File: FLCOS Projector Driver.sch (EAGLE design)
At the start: 64 parts, among them IC2 LM3414, IC3 MIC5219BM5, IC4 MIC5219BM5, IC5 LM3414, IC6 LM3414, Q1 14.31818MHz, Q3 12MHz, T2 S8050, T3 S8050, U1 TVP5150-NTSC_DECODER, U2 ESP32-WROOM-32U, U9 CH340G, X1 FH12-25S-0.5SH

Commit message: Started BOM. Changing parts to Mouser in-stock
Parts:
- removed Q1: 14.31818MHz, crystal:CRYSTALCTS406
- removed T3: S8050, transistor:BC846
- removed U$10: MICROSD, micro-sd:MICROSD
- removed U1: TVP5150-NTSC_DECODER, SparkFun-AnalogIC:TVP5150-NTSC_DECODER
- removed U2: ESP32-WROOM-32U, ESP32-WROOM-32U:ESP32-WROOM-32U
- removed U9: CH340G, usb-serial:CH340G
- added FPC: FH12-25S-0.5SH, con-hirose:FH12-25S-0.5SH
- added IC7, IC8, IC9: LM3414, A_butts:LM3414SO08-PAD
- added J1: MEM2075-00-140-01-A, MEM2075-00-140-01-A:MEM2075-00-140-01-A
- added T1: S8050, transistor:BC846
- C47, C56: value 0.1uF -> 100nF
- IC1: value (none) -> LM1117MPX-3.3
- IC2: value LM3414 -> MIC5219BM5; device A_butts:LM3414SO08-PAD -> v-reg-micrel:MIC5219BM5
- IC4: value MIC5219BM5 -> TVP5150-NTSC_DECODER; device v-reg-micrel:MIC5219BM5 -> SparkFun-AnalogIC:TVP5150-NTSC_DECODER
- IC5: value LM3414 -> CH340G; device A_butts:LM3414SO08-PAD -> usb-serial:CH340G
- IC6: value LM3414 -> ESP32-WROOM-32U; device A_butts:LM3414SO08-PAD -> ESP32-WROOM-32U:ESP32-WROOM-32U
- L1, L2, L5: value 15uF -> 15uH
- R67: value 4K7 -> 2K2
- X1: value FH12-25S-0.5SH -> 14.31818MHz; device con-hirose:FH12-25S-0.5SH -> crystal:CRYSTALCTS406
- renumbered D5 to D3, Q3 to X2
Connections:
- removed net N$1 (its old number): IC4.ADJ
- new net N$16: IC2.ADJ
- net +1V8: now also IC2.OUT, IC4.CH_AVDD, IC4.DVDD, IC4.PLL_AVDD; no longer IC3.OUT, U1.CH_AVDD, U1.DVDD, U1.PLL_AVDD
- net +2V5: now also FPC-25.1, IC3.OUT; no longer IC4.OUT, X1-25.1
- net +3V3: now also IC4.IO_DVDD, IC4.PDN, IC6.3V3, J1.VDD; no longer U$10.VDD, U1.IO_DVDD, U1.PDN, U2.3V3
- net +5V: now also FPC-1.1, FPC-11.1, IC2.EN, IC2.IN, IC5.VCC, IC7.VIN, IC8.VIN, IC9.VIN; no longer IC2.VIN, IC4.EN, IC4.IN, IC5.VIN, IC6.VIN, U9.VCC, X1-1.1, X1-11.1
- net AIP1A: now also IC4.AIP1A; no longer U1.AIP1A
- net AIP1B: now also IC4.AIP1B; no longer U1.AIP1B
- net BLU_PWM: now also FPC-14.1, IC9.DIM; no longer IC5.DIM, X1-14.1
- net ESP_EN_N: now also FPC-23.1, IC6.EN, T2.C; no longer T3.C, U2.EN, X1-23.1
- net ESP_RX: now also IC6.RXD0; no longer U2.RXD0
- net ESP_TX: now also IC6.TXD0; no longer U2.TXD0
- net FLCOS_CS_N: now also FPC-3.1, IC6.IO4; no longer U2.IO4, X1-3.1
- net FLCOS_D0: now also FPC-18.1, IC4.YOUT_0, IC6.IO27; no longer U1.YOUT_0, U2.IO27, X1-18.1
- net FLCOS_D1: now also FPC-17.1, IC4.YOUT_1, IC6.IO14; no longer U1.YOUT_1, U2.IO14, X1-17.1
- net FLCOS_D2: now also FPC-16.1, IC4.YOUT_2, IC6.IO12; no longer U1.YOUT_2, U2.IO12, X1-16.1
- net FLCOS_D3: now also FPC-15.1, IC4.YOUT_3, IC6.IO13; no longer U1.YOUT_3, U2.IO13, X1-15.1
- net FLCOS_D4: now also FPC-10.1, IC4.YOUT_4, IC6.IO22; no longer U1.YOUT_4, U2.IO22, X1-10.1
- net FLCOS_D5: now also FPC-9.1, IC4.YOUT_5, IC6.IO21; no longer U1.YOUT_5, U2.IO21, X1-9.1
- net FLCOS_D6: now also FPC-8.1, IC4.YOUT_6, IC6.IO17; no longer U1.YOUT_6, U2.IO17, X1-8.1
- net FLCOS_D7: now also FPC-7.1, IC4.YOUT_7, IC6.IO16; no longer U1.YOUT_7, U2.IO16, X1-7.1
- net FLCOS_HD: now also FPC-21.1, IC4.HSYNC, IC6.IO33; no longer U1.HSYNC, U2.IO33, X1-21.1
- net FLCOS_PCLK: now also FPC-22.1, IC4.PCLK/SCLK, IC6.IO32; no longer U1.PCLK/SCLK, U2.IO32, X1-22.1
- net FLCOS_SOUT: now also FPC-5.1; no longer X1-5.1
- net FLCOS_VALID: now also FPC-19.1, IC4.AVID, IC6.IO26; no longer U1.AVID, U2.IO26, X1-19.1
- net FLCOS_VD: now also FPC-20.1, IC4.VSYNC, IC6.IO25; no longer U1.VSYNC, U2.IO25, X1-20.1
- net GND: now also FPC-2.1, FPC-24.1, IC4.AGND, IC4.CH_AGND, IC4.DGND, IC4.PLL_AGND, IC6.GND@1, IC6.GND@15, IC6.GND@38, IC6.GND@THERM, IC7.EP, IC7.GND, IC7.PGND, IC8.EP, IC8.GND, IC8.PGND, IC9.EP, IC9.GND, IC9.PGND, J1.SHIELD, J1.VSS; no longer IC2.EP, IC2.PGND, IC4.GND, IC5.EP, IC5.PGND, IC6.EP, IC6.GND, IC6.PGND, U$10.GND, U$10.SHIELD@1, U$10.SHIELD@2, U$10.SHIELD@3, U$10.SHIELD@4, U1.AGND, U1.CH_AGND, U1.DGND, U1.PLL_AGND, U2.GND@1, U2.GND@15, U2.GND@38, U2.GND@THERM, U9.GND, X1-2.1, X1-24.1
- net GRN_PWM: now also FPC-13.1, IC8.DIM; no longer IC6.DIM, X1-13.1
- net N$2: now also IC7.IADJ; no longer IC2.IADJ
- net N$24: now also IC8.IADJ; no longer IC6.IADJ
- net N$25: now also IC8.FS; no longer IC6.FS
- net N$26: now also IC8.VCC; no longer IC6.VCC
- net N$27: now also IC8.LX; no longer IC6.LX
- net N$3: now also IC7.FS; no longer IC2.FS
- net N$4: now also IC7.VCC; no longer IC2.VCC
- net N$5: now also IC7.LX; no longer IC2.LX
- net N$6: now also IC9.IADJ; no longer IC5.IADJ
- net N$67: now also IC5.TX; no longer U9.TX
- net N$7: now also IC9.FS; no longer IC5.FS
- net N$70: now also IC5.RX; no longer U9.RX
- net N$71: now also T1.B; no longer T2.B
- net N$77: now also T2.B; no longer T3.B
- net N$78: now also IC5.RTS, T2.E; no longer T3.E, U9.RTS
- net N$79: now also IC5.DTR, T1.E; no longer T2.E, U9.DTR
- net N$8: now also IC9.VCC; no longer IC5.VCC
- net N$80: now also IC5.V3; no longer U9.V3
- net N$81: now also IC5.XI; no longer U9.XI
- net N$82: now also IC5.XO; no longer U9.XO
- net N$9: now also IC9.LX; no longer IC5.LX
- net RED_PWM: now also FPC-12.1, IC7.DIM; no longer IC2.DIM, X1-12.1
- net REFM: now also IC4.REFM; no longer U1.REFM
- net REFP: now also IC4.REFP; no longer U1.REFP
- net SD_CS_N: now also IC6.IO5, J1.CD/DAT3; no longer U$10.CD/DAT3/CS, U2.IO5
- net SPI_MISO: now also IC6.IO19, J1.DAT0; no longer U$10.DAT0/DO, U2.IO19
- net SPI_MOSI: now also FPC-6.1, IC6.IO23, J1.CMD; no longer U$10.CMD/DI, U2.IO23, X1-6.1
- net SPI_SCLK: now also FPC-4.1, IC6.IO18, J1.CLK; no longer U$10.CLK/SCLK, U2.IO18, X1-4.1
- net TVP_FID: now also IC4.FID/GLCO, IC6.IO34; no longer U1.FID/GLCO, U2.IO34
- net TVP_FL_RST_N: now also IC4.RESET/, IC6.IO0, T1.C; no longer T2.C, U1.RESET/, U2.IO0
- net TVP_INT: now also IC4.INT_REQ, IC6.IO35; no longer U1.INT_REQ, U2.IO35
- net TVP_SCL: now also IC4.SCL, IC6.IO15; no longer U1.SCL, U2.IO15
- net TVP_SDA: now also IC4.SDA, IC6.IO2; no longer U1.SDA, U2.IO2
- net USB_D+: now also IC5.D+; no longer U9.D+
- net USB_D-: now also IC5.D-; no longer U9.D-
- net XTAL1: now also IC4.XTAL1, X1.2; no longer Q1.2, U1.XTAL1
- net XTAL2: now also IC4.XTAL2, X1.1; no longer Q1.1, U1.XTAL2

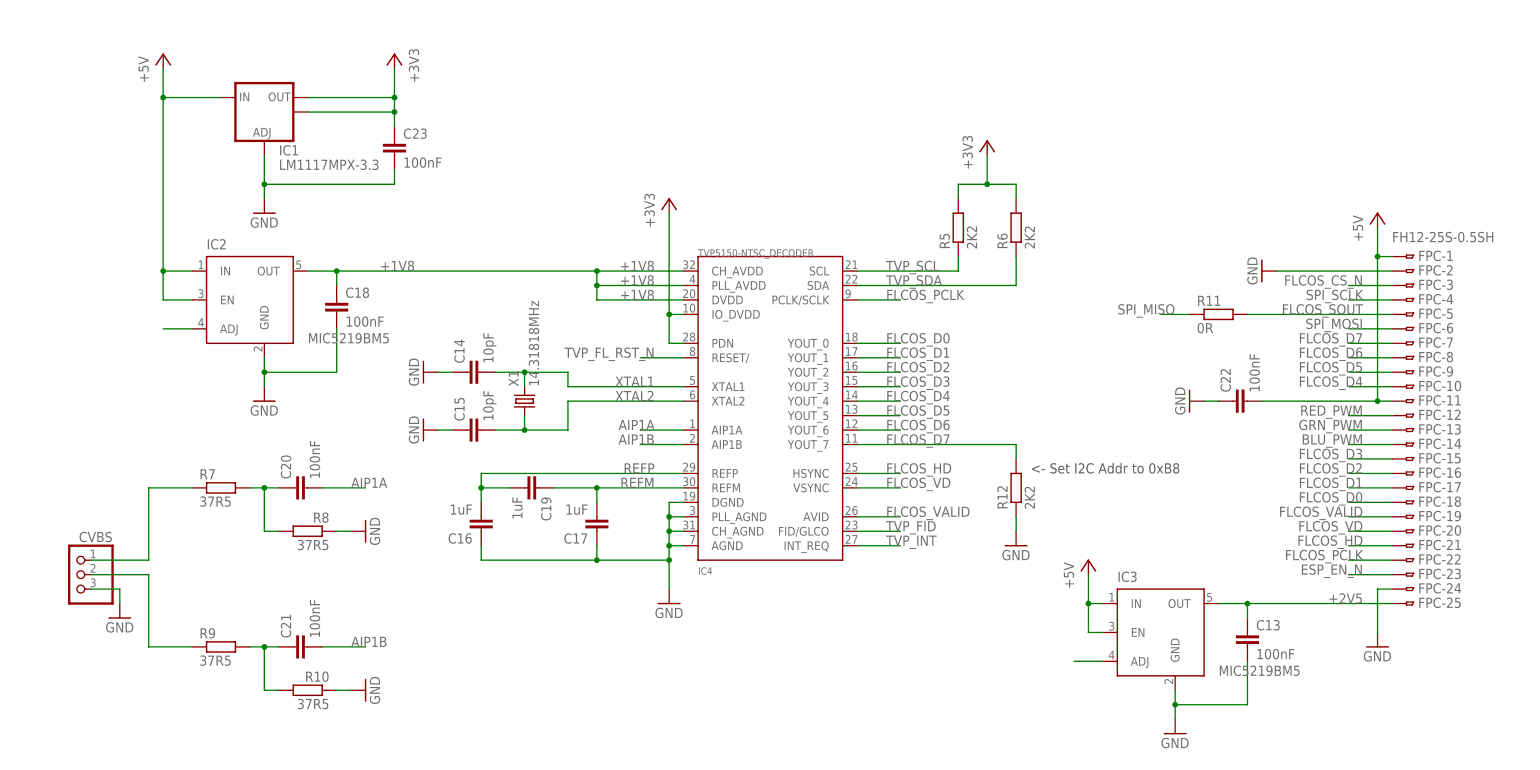
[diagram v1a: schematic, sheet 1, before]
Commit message: ERC and DRC passed. BOM not quite done
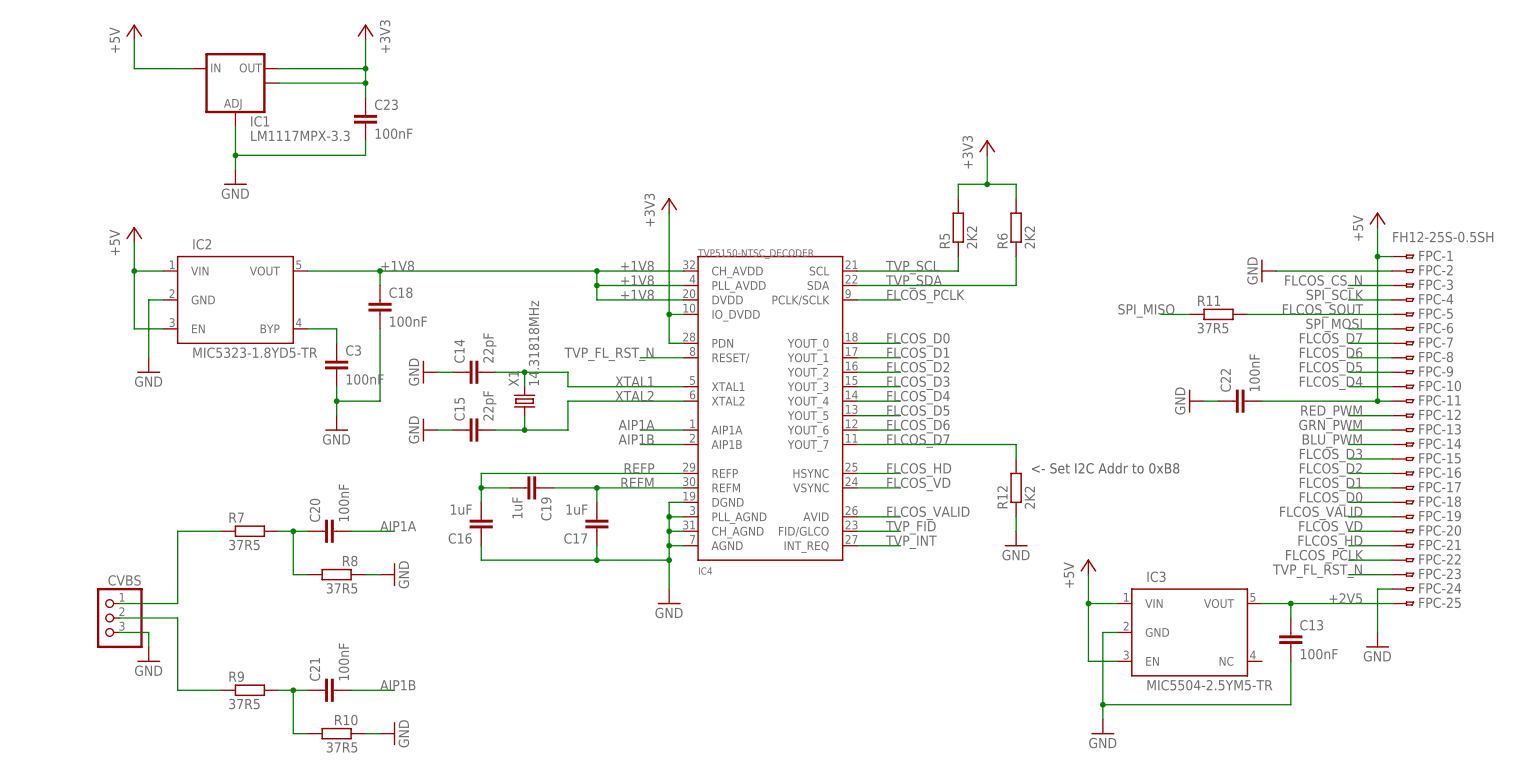
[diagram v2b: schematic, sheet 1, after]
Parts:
- removed L5: 15uH, A_butts:INDUCTOR-TAIYO-YUDEN-6X2.8
- added C3: 100nF, rcl:C-EUC0603
- added L3: 15uH, A_butts:INDUCTOR-TAIYO-YUDEN-6X2.8
- C14, C15: value 10pF -> 22pF
- D1, D2, D3: value (none) -> "SB34AFC-AU_R1_000A1 SB34AFC-AU_R1_000A1"
- IC2: value MIC5219BM5 -> MIC5323-1.8YD5-TR; device v-reg-micrel:MIC5219BM5 -> v-reg-micrel:MIC5323-1.8YD5-TR
- IC3: value MIC5219BM5 -> MIC5504-2.5YM5-TR; device v-reg-micrel:MIC5219BM5 -> v-reg-micrel:MIC5504-2.5YM5-TR
- R11: value 0R -> 37R5
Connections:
- removed net N$1: IC3.ADJ
- removed net N$16: IC2.ADJ
- new net N$10: C3.1, IC2.BYP
- net +1V8: now also IC2.VOUT; no longer IC2.OUT
- net +2V5: now also IC3.VOUT; no longer IC3.OUT
- net +5V: now also IC2.VIN, IC3.VIN; no longer IC2.IN, IC3.IN
- net BLU_CATHODE: now also L3.2; no longer L2.2
- net ESP_EN_N: no longer FPC-23.1
- net GND: now also C3.2
- net GRN_CATHODE: now also L2.2; no longer L5.2
- net N$27: now also L2.1; no longer L5.1
- net N$9: now also L3.1; no longer L2.1
- net TVP_FL_RST_N: now also FPC-23.1
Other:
- note added: "Included RGB LED from AliExpress FLCOS. Pinout and LED colours tested with meter and bench PSU. Please ignore the silkscreen markings on the FLCOS module's LED board."
- note removed: "Included RGB LED from AliExpress FLCOS. Pinout / LED colours tested with meter and bench PSU. Please ignore the silkscreen markings on the FLCOS module's LED board."
- moved on the sheet: C13, C18, C20, C21, C23, CVBS, IC1, L2, R10, R7, R8, R9

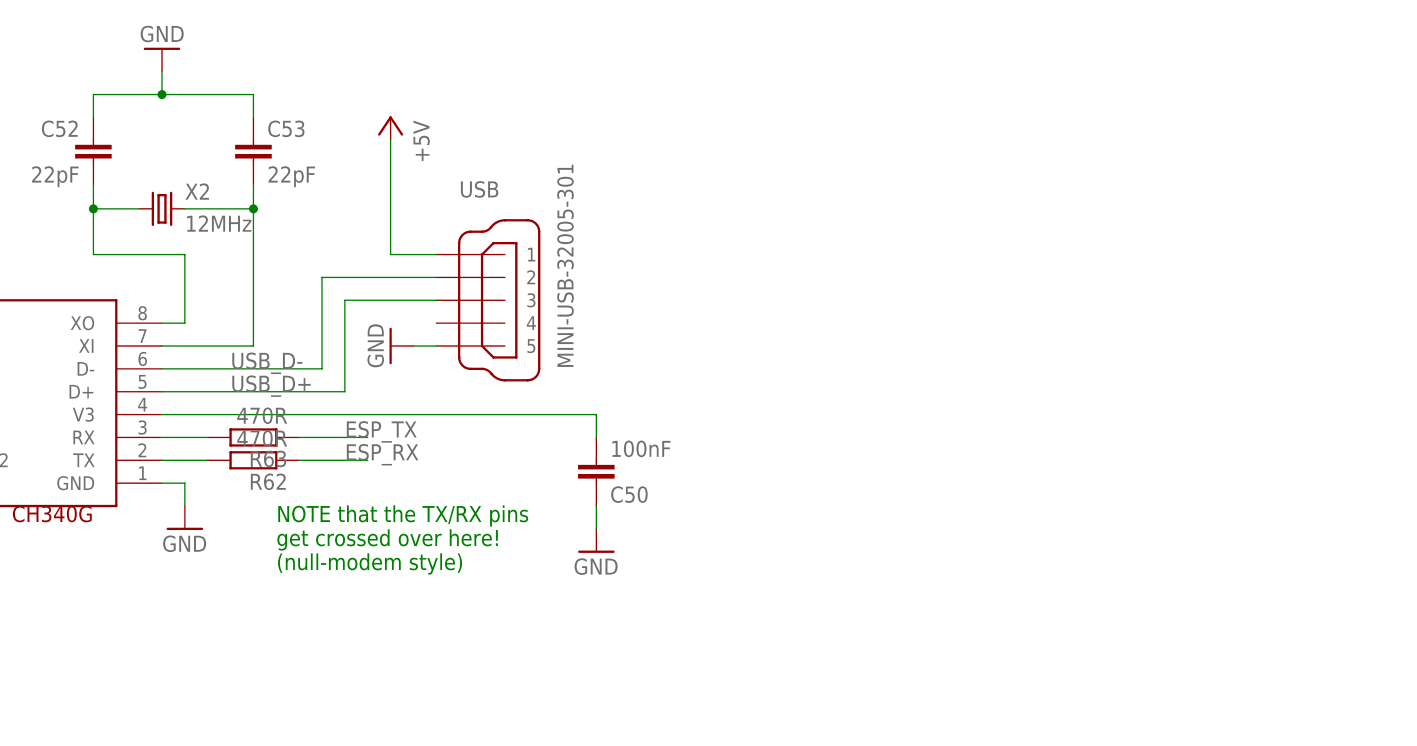
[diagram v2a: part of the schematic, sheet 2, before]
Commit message: Changed to USB-C. BOM passives not done yet
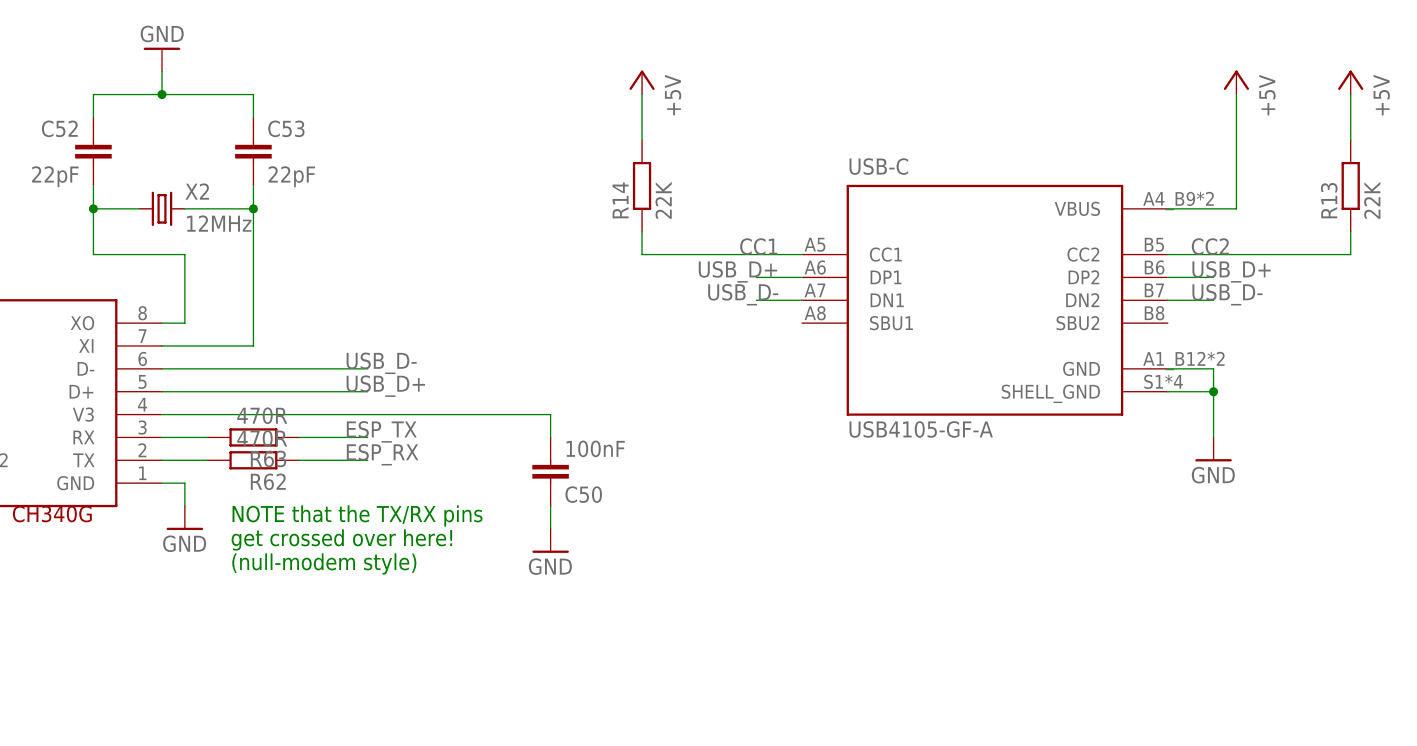
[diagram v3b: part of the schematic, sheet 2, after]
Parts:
- removed USB: MINI-USB-32005-301, con-cypressindustries:MINI-USB-32005-301
- added R13, R14: 22K, rcl:R-EU_R0603
- added USB-C: USB4105-GF-A, USB4105-GF-A:USB4105-GF-A
- R16, R2, R4: value 20K -> 22K
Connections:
- new net CC1: R14.1, USB-C.CC1
- new net CC2: R13.1, USB-C.CC2
- net +5V: now also R13.2, R14.2, USB-C.VBUS; no longer USB.1
- net GND: now also USB-C.GND, USB-C.SHELL_GND; no longer USB.5
- net USB_D+: now also USB-C.DP1, USB-C.DP2; no longer USB.3
- net USB_D-: now also USB-C.DN1, USB-C.DN2; no longer USB.2
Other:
- note added: "Examples... RIADJ = 33K = 94.7 mA RIADJ = 22K = 142.04 mA RIADJ = 15K = 208.3 mA"
- note removed: "Examples... RIADJ = 33K = 94.7 mA RIADJ = 20K = 156.25 mA RIADJ = 15K = 208.3 mA"
- moved on the sheet: C50

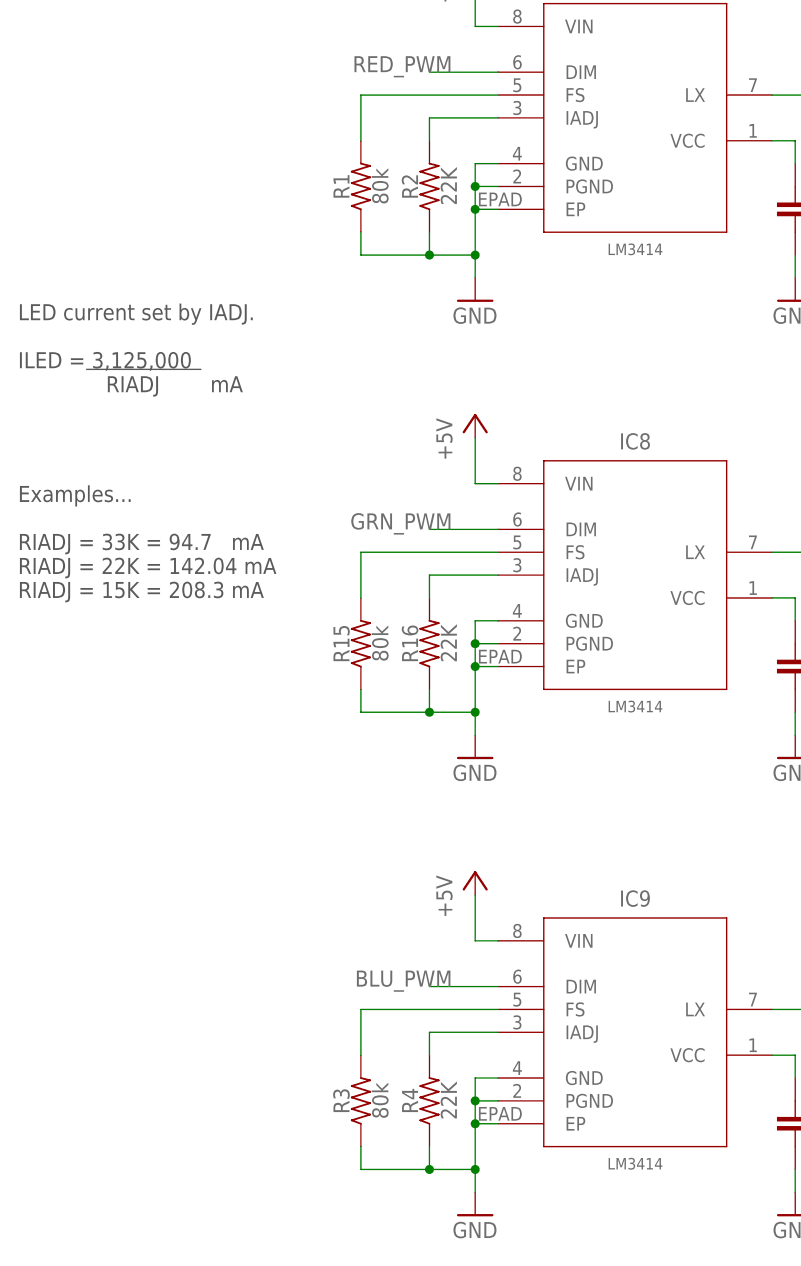
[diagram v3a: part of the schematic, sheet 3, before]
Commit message: Changed Composite pin header for TRRS socket
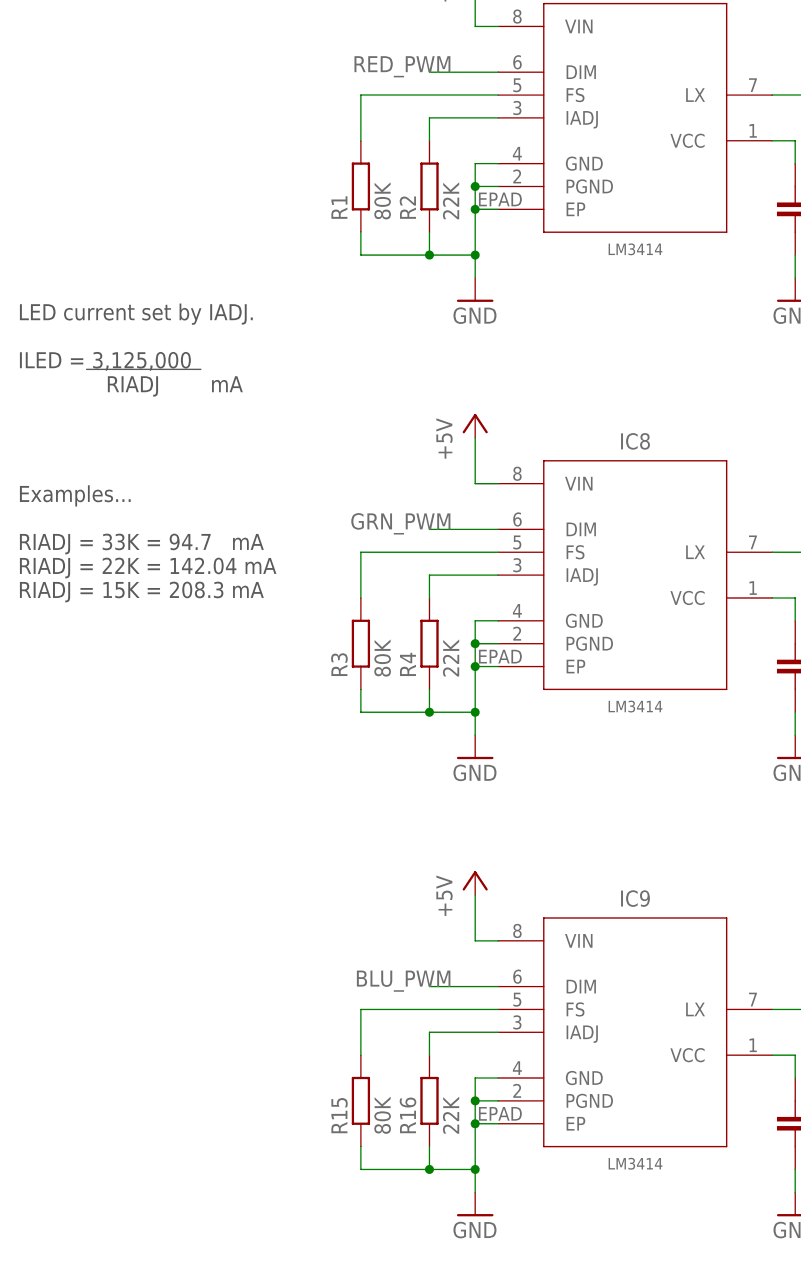
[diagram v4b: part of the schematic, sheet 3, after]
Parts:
- CVBS: value (none) -> AUDIO_JACK_TRRSSMD_RA; device pinhead:PINHD-1X3 -> SparkFun-Connectors:AUDIO_JACK_TRRSSMD_RA
- R1, R15, R3: value 80k -> 80K; device A_butts:RESISTORR0603 -> rcl:R-EU_R0603
- R16, R2, R4: device A_butts:RESISTORR0603 -> rcl:R-EU_R0603
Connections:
- net GND: now also CVBS.EARTH; no longer CVBS.3
- net N$20: now also CVBS.TIP; no longer CVBS.1
- net N$21: now also CVBS.RING2; no longer CVBS.2
- net N$24: now also R4.2; no longer R16.2
- net N$25: now also R3.2; no longer R15.2
- net N$6: now also R16.2; no longer R4.2
- net N$7: now also R15.2; no longer R3.2
